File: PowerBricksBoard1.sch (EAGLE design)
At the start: 16 parts

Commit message: test
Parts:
- removed U$6: BRICKBOARD_TSW_14X2, Dist_to_Brickboard_Connector_brick:BRICKBOARD_TSW_14X2
- added U$2: BRICK2DIST, Brick_Dist_Connector:BRICK2DIST
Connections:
- net 12V: now also U$2.VOUT+; no longer U$6.45, U$6.46, U$6.47, U$6.48, U$6.49, U$6.50, U$6.51, U$6.52, U$6.53, U$6.54, U$6.55, U$6.56
- net 12_GND: now also U$2.VOUT-; no longer U$6.29, U$6.30, U$6.31, U$6.32, U$6.33, U$6.34, U$6.35, U$6.36, U$6.37, U$6.38, U$6.39, U$6.40
- net 48V: now also U$2.VIN+; no longer U$6.15, U$6.16, U$6.17, U$6.18, U$6.19, U$6.20, U$6.21, U$6.22, U$6.23, U$6.24, U$6.25, U$6.26, U$6.27, U$6.28
- net 48_GND: now also U$2.VIN-; no longer U$6.10, U$6.11, U$6.12, U$6.13, U$6.14, U$6.3, U$6.4, U$6.5, U$6.6, U$6.7, U$6.8, U$6.9
- net ALERT: now also U$2.ALERT; no longer U$6.43
- net CLK: now also U$2.CLK; no longer U$6.44
- net DATA: now also U$2.DATA; no longer U$6.42
- net ON/OFF: now also U$2.C2, U$2.ON/OFF; no longer U$6.1
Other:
- note added: "ADDR1 = R3 Resistor ADDR0 = R4 Resistor Octal Address = 8*ADDR1 + ADDR0 0-12 and 40, 44, 45, and 55 address can’t be used (decimal)"
- note added: "Backplane Connector"
- note added: "Brick Connections"
- note removed: "ADDR1 = R3 Resistor ADDR0 = R4 Resistor Octal Address = 8*ADDR1 + ADDR0"
- moved on the sheet: C1, C2, C3, D1, D2, H1, H2, H3, H4, R1, R2, R3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

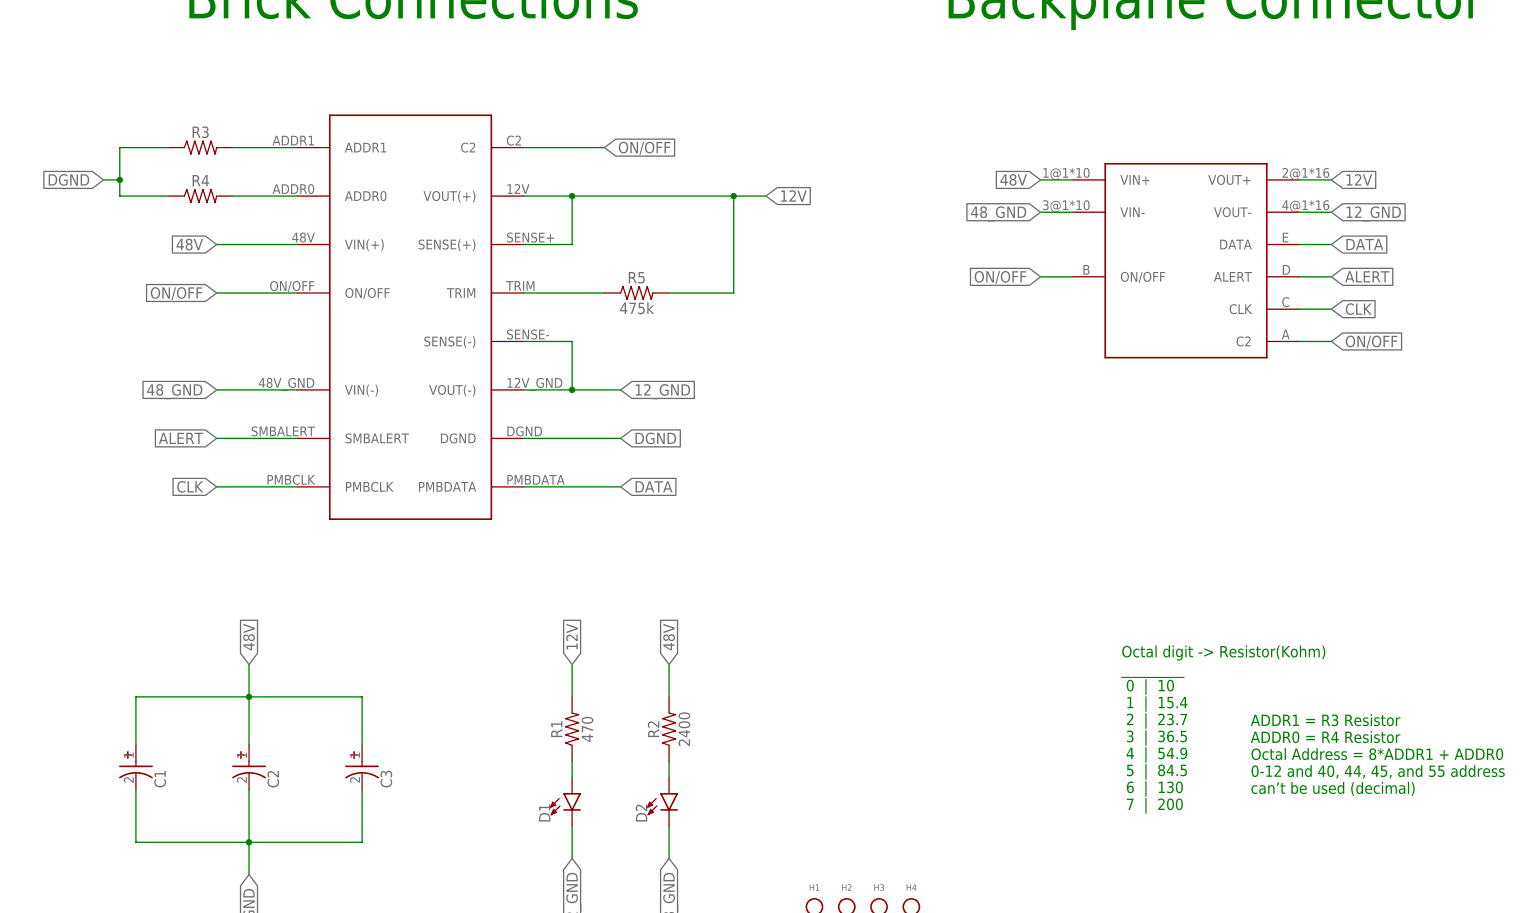
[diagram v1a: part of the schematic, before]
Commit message: cad placement for tyler (routing not done)
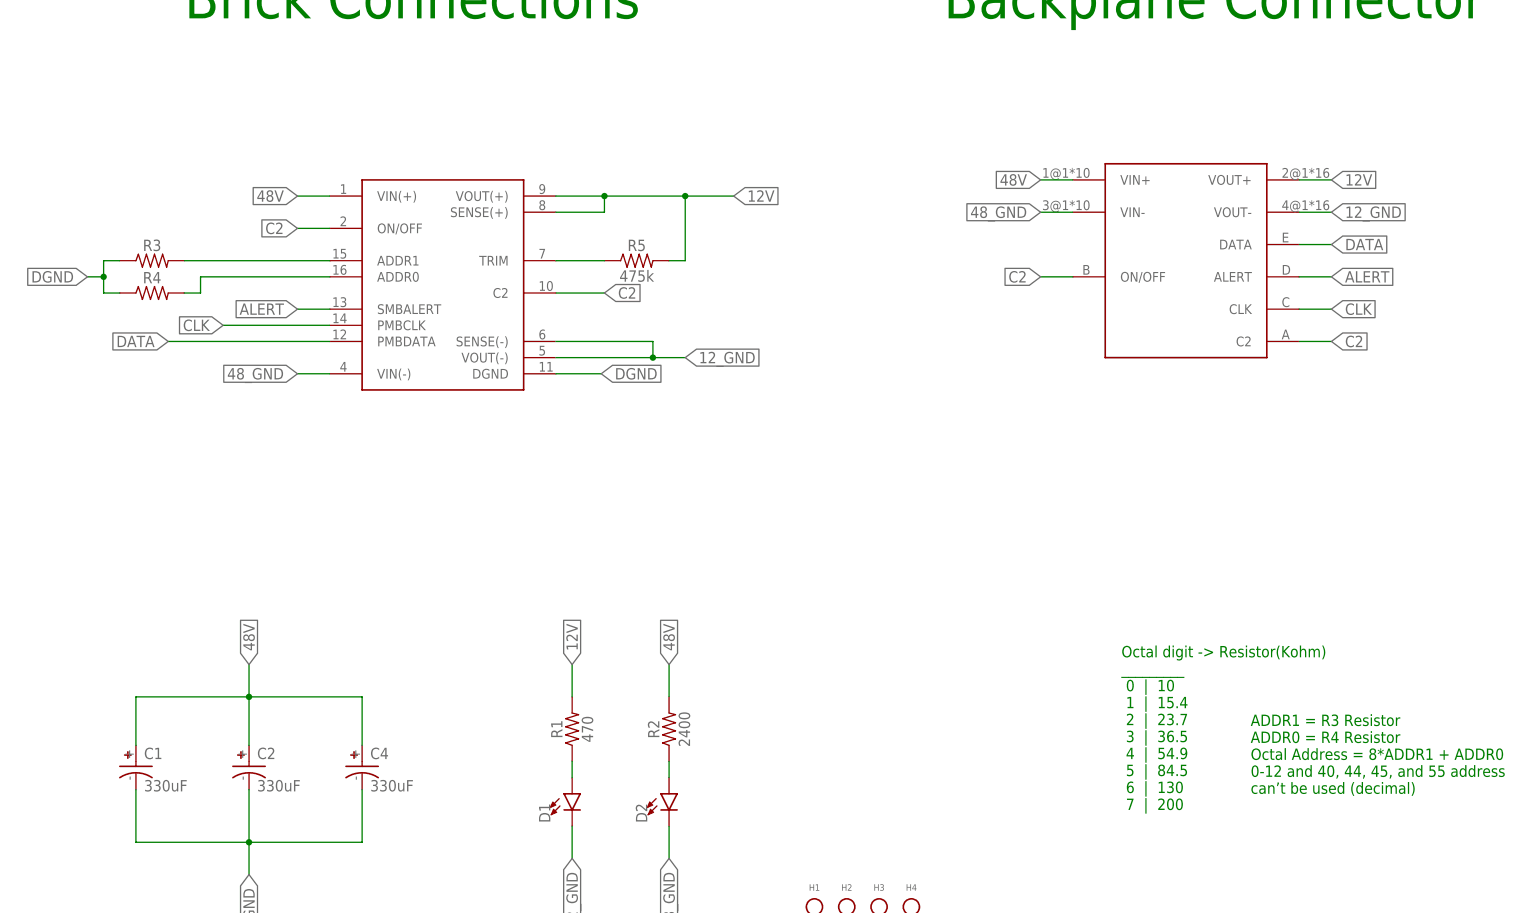
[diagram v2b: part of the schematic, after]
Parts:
- removed C3: UCM1H331MNL1GS, UCM1H331MNL1GS:UCM1H331MNL1GS
- removed U$1: Q48SC12050NRDH, Q48SC12050NRDH:Q48SC12050NRDH
- added C4: 330uF, brick-capacitor-UCM1H331MNL1GS:UCM1H331MNL1GS
- added U$3: BRICK2DIST_C, Brick_Dist_Connector:BRICK2DIST_C
- C1, C2: value UCM1H331MNL1GS -> 330uF; device UCM1H331MNL1GS:UCM1H331MNL1GS -> brick-capacitor-UCM1H331MNL1GS:UCM1H331MNL1GS
- U$2: value BRICK2DIST -> Q48SC12050NRDH; device Brick_Dist_Connector:BRICK2DIST -> Delta Power Bricks - Q48SC12050NRDH:Q48SC12050NRDH
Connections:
- removed net ON/OFF: U$1.C2, U$1.ON/OFF, U$2.C2, U$2.ON/OFF
- new net C2: U$2.C2, U$2.ON/OFF, U$3.C2, U$3.ON/OFF
- net 12V: now also U$2.SENSE(+), U$2.VOUT(+), U$3.VOUT+; no longer U$1.SENSE(+), U$1.VOUT(+), U$2.VOUT+
- net 12_GND: now also U$2.SENSE(-), U$2.VOUT(-), U$3.VOUT-; no longer U$1.SENSE(-), U$1.VOUT(-), U$2.VOUT-
- net 48V: now also C4.+, U$2.VIN(+), U$3.VIN+; no longer C3.+, U$1.VIN(+), U$2.VIN+
- net 48_GND: now also C4.-, U$2.VIN(-), U$3.VIN-; no longer C3.-, U$1.VIN(-), U$2.VIN-
- net ALERT: now also U$2.SMBALERT, U$3.ALERT; no longer U$1.SMBALERT, U$2.ALERT
- net CLK: now also U$2.PMBCLK, U$3.CLK; no longer U$1.PMBCLK, U$2.CLK
- net DATA: now also U$2.PMBDATA, U$3.DATA; no longer U$1.PMBDATA, U$2.DATA
- net DGND: now also U$2.DGND; no longer U$1.DGND
- net N$3: now also U$2.ADDR1; no longer U$1.ADDR1
- net N$4: now also U$2.ADDR0; no longer U$1.ADDR0
- net N$5: now also U$2.TRIM; no longer U$1.TRIM
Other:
- moved on the sheet: C1, C2, R3, R4, R5

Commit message: Owo
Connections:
- new net ON/OFF: U$2.ON/OFF, U$3.ON/OFF
- net C2: no longer U$2.ON/OFF, U$3.ON/OFF
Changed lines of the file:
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@@
 <net name="C2" class="0">
-<segment>
-<wire x1="48.26" y1="35.56" x2="43.18" y2="35.56" width="0.1524" layer="91"/>
-<label x="43.18" y="35.56" size="1.778" layer="95" rot="R180" xref="yes"/>
-<pinref part="U$3" gate="G$1" pin="ON/OFF"/>
-</segment>
 <segment>
 <wire x1="83.82" y1="25.4" x2="88.9" y2="25.4" width="0.1524" layer="91"/>
@@
 <label x="-25.4" y="33.02" size="1.778" layer="95" xref="yes"/>
 <pinref part="U$2" gate="G$1" pin="C2"/>
-</segment>
-<segment>
-<wire x1="-68.58" y1="43.18" x2="-73.66" y2="43.18" width="0.1524" layer="91"/>
-<label x="-73.66" y="43.18" size="1.778" layer="95" rot="R180" xref="yes"/>
-<pinref part="U$2" gate="G$1" pin="ON/OFF"/>
 </segment>
 </net>
@@
 </segment>
 </net>
+<net name="ON/OFF" class="0">
+<segment>
+<wire x1="-68.58" y1="43.18" x2="-73.66" y2="43.18" width="0.1524" layer="91"/>
+<label x="-73.66" y="43.18" size="1.778" layer="95" rot="R180" xref="yes"/>
+<pinref part="U$2" gate="G$1" pin="ON/OFF"/>
+</segment>
+<segment>
+<wire x1="48.26" y1="35.56" x2="43.18" y2="35.56" width="0.1524" layer="91"/>
+<label x="43.18" y="35.56" size="1.778" layer="95" rot="R180" xref="yes"/>
+<pinref part="U$3" gate="G$1" pin="ON/OFF"/>
+</segment>
+</net>

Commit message: Done but I still need to add a picture Owo
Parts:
- removed U$3: BRICK2DIST_C, Brick_Dist_Connector:BRICK2DIST_C
- added U$1: BRICK2DIST, Brick_Dist_Connector:BRICK2DIST
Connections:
- net 12V: now also U$1.VOUT+; no longer U$3.VOUT+
- net 12_GND: now also U$1.VOUT-; no longer U$3.VOUT-
- net 48V: now also U$1.VIN+; no longer U$3.VIN+
- net 48_GND: now also U$1.VIN-; no longer U$3.VIN-
- net ALERT: now also U$1.ALERT; no longer U$3.ALERT
- net C2: now also U$1.C2; no longer U$3.C2
- net CLK: now also U$1.CLK; no longer U$3.CLK
- net DATA: now also U$1.DATA; no longer U$3.DATA
- net ON/OFF: now also U$1.ON/OFF; no longer U$3.ON/OFF
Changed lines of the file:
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@@
 <part name="H3" library="Mounting Holes" deviceset="6-32-HOLE" device="" package3d_urn="urn:adsk.eagle:package:24384748/2"/>
 <part name="H4" library="Mounting Holes" deviceset="6-32-HOLE" device="" package3d_urn="urn:adsk.eagle:package:24384748/2"/>
-<part name="U$3" library="Brick_Dist_Connector" deviceset="BRICK2DIST_C" device=""/>
 <part name="C1" library="brick-capacitor-UCM1H331MNL1GS" deviceset="UCM1H331MNL1GS" device="" package3d_urn="urn:adsk.eagle:package:24202090/2" value="330uF"/>
 <part name="C2" library="brick-capacitor-UCM1H331MNL1GS" deviceset="UCM1H331MNL1GS" device="" package3d_urn="urn:adsk.eagle:package:24202090/2" value="330uF"/>
@@
 <part name="R3" library="SparkFun-Resistors" library_urn="urn:adsk.eagle:library:532" deviceset="RESISTOR" device="0603" package3d_urn="urn:adsk.eagle:package:39650/1" value=" "/>
 <part name="R5" library="SparkFun-Resistors" library_urn="urn:adsk.eagle:library:532" deviceset="RESISTOR" device="0603" package3d_urn="urn:adsk.eagle:package:39650/1" value="475k"/>
+<part name="U$1" library="Brick_Dist_Connector" deviceset="BRICK2DIST" device=""/>
 </parts>
 <sheets>
@@
 <attribute name="VALUE" x="22.86" y="-66.04" size="1.016" layer="95" align="top-center"/>
 </instance>
-<instance part="U$3" gate="G$1" x="53.34" y="45.72" smashed="yes"/>
 <instance part="C1" gate="G$1" x="-99.06" y="-40.64" smashed="yes">
 <attribute name="NAME" x="-97.79" y="-39.37" size="1.778" layer="95" align="center-left"/>
@@
 <attribute name="NAME" x="-20.32" y="39.624" size="1.778" layer="95" font="vector" align="bottom-center"/>
 <attribute name="VALUE" x="-20.32" y="36.576" size="1.778" layer="96" font="vector" align="top-center"/>
+</instance>
+<instance part="U$1" gate="G$1" x="53.34" y="45.72" smashed="yes">
+<attribute name="NAME" x="53.848" y="54.356" size="1.778" layer="95"/>
 </instance>
 </instances>
@@
 <wire x1="48.26" y1="50.8" x2="43.18" y2="50.8" width="0.1524" layer="91"/>
 <label x="43.18" y="50.8" size="1.778" layer="95" rot="R180" xref="yes"/>
-<pinref part="U$3" gate="G$1" pin="VIN+"/>
+<pinref part="U$1" gate="G$1" pin="VIN+"/>
 </segment>
 <segment>
@@
 <wire x1="48.26" y1="45.72" x2="43.18" y2="45.72" width="0.1524" layer="91"/>
 <label x="43.18" y="45.72" size="1.778" layer="95" rot="R180" xref="yes"/>
-<pinref part="U$3" gate="G$1" pin="VIN-"/>
+<pinref part="U$1" gate="G$1" pin="VIN-"/>
 </segment>
 <segment>
@@
 <wire x1="83.82" y1="50.8" x2="88.9" y2="50.8" width="0.1524" layer="91"/>
 <label x="88.9" y="50.8" size="1.778" layer="95" xref="yes"/>
-<pinref part="U$3" gate="G$1" pin="VOUT+"/>
+<pinref part="U$1" gate="G$1" pin="VOUT+"/>
 </segment>
 <segment>
@@
 <wire x1="83.82" y1="25.4" x2="88.9" y2="25.4" width="0.1524" layer="91"/>
 <label x="88.9" y="25.4" size="1.778" layer="95" xref="yes"/>
-<pinref part="U$3" gate="G$1" pin="C2"/>
+<pinref part="U$1" gate="G$1" pin="C2"/>
 </segment>
 <segment>
@@
 <wire x1="83.82" y1="45.72" x2="88.9" y2="45.72" width="0.1524" layer="91"/>
 <label x="88.9" y="45.72" size="1.778" layer="95" xref="yes"/>
-<pinref part="U$3" gate="G$1" pin="VOUT-"/>
+<pinref part="U$1" gate="G$1" pin="VOUT-"/>
 </segment>
 <segment>
@@
 <wire x1="83.82" y1="35.56" x2="88.9" y2="35.56" width="0.1524" layer="91"/>
 <label x="88.9" y="35.56" size="1.778" layer="95" xref="yes"/>
-<pinref part="U$3" gate="G$1" pin="ALERT"/>
+<pinref part="U$1" gate="G$1" pin="ALERT"/>
 </segment>
 <segment>
@@
 <wire x1="83.82" y1="40.64" x2="88.9" y2="40.64" width="0.1524" layer="91"/>
 <label x="88.9" y="40.64" size="1.778" layer="95" xref="yes"/>
-<pinref part="U$3" gate="G$1" pin="DATA"/>
+<pinref part="U$1" gate="G$1" pin="DATA"/>
 </segment>
 <segment>
@@
 <wire x1="83.82" y1="30.48" x2="88.9" y2="30.48" width="0.1524" layer="91"/>
 <label x="88.9" y="30.48" size="1.778" layer="95" xref="yes"/>
-<pinref part="U$3" gate="G$1" pin="CLK"/>
+<pinref part="U$1" gate="G$1" pin="CLK"/>
 </segment>
 <segment>
@@
 <wire x1="48.26" y1="35.56" x2="43.18" y2="35.56" width="0.1524" layer="91"/>
 <label x="43.18" y="35.56" size="1.778" layer="95" rot="R180" xref="yes"/>
-<pinref part="U$3" gate="G$1" pin="ON/OFF"/>
-</segment>
-</net>
+<pinref part="U$1" gate="G$1" pin="ON/OFF"/>
+</segment>
+</net>

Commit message: owo
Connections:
- net 48V renamed 48V_GND
- net N$3 renamed ADDR1
- net N$4 renamed ADDR0
- net N$5 renamed TRIM
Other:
- note added: "Trim up: 5.11 * 12 (100+ Delta )/(1.225* Delta) - 511/Delta - 10.2 = resistor to use in kOhm Where Delta is the % up for trim (10% = 10)"
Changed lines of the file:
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@@
 <text x="-91.44" y="76.2" size="6.4516" layer="91">Brick Connections</text>
 <text x="27.94" y="76.2" size="6.4516" layer="91">Backplane Connector</text>
+<text x="55.88" y="-17.78" size="1.778" layer="91">Trim up: 5.11 * 12 (100+ Delta )/(1.225* Delta)
+- 511/Delta - 10.2 = resistor to use in kOhm
+Where Delta is the % up for trim (10% = 10) </text>
 </plain>
 <instances>
@@
 </busses>
 <nets>
-<net name="48V" class="0">
+<net name="48V_GND" class="0">
 <segment>
 <wire x1="-99.06" y1="-30.48" x2="-81.28" y2="-30.48" width="0.1524" layer="91"/>
@@
 </segment>
 </net>
-<net name="N$3" class="0">
+<net name="ADDR1" class="0">
 <segment>
 <wire x1="-91.44" y1="38.1" x2="-68.58" y2="38.1" width="0.1524" layer="91"/>
 <pinref part="R3" gate="G$1" pin="2"/>
 <pinref part="U$2" gate="G$1" pin="ADDR1"/>
-</segment>
-</net>
-<net name="N$4" class="0">
+<label x="-88.9" y="38.1" size="1.778" layer="95"/>
+</segment>
+</net>
+<net name="ADDR0" class="0">
 <segment>
 <pinref part="U$2" gate="G$1" pin="ADDR0"/>
@@
 <pinref part="R4" gate="G$1" pin="2"/>
 <wire x1="-88.9" y1="33.02" x2="-91.44" y2="33.02" width="0.1524" layer="91"/>
-</segment>
-</net>
-<net name="N$5" class="0">
+<label x="-88.9" y="35.56" size="1.778" layer="95"/>
+</segment>
+</net>
+<net name="TRIM" class="0">
 <segment>
 <wire x1="-25.4" y1="38.1" x2="-33.02" y2="38.1" width="0.1524" layer="91"/>
 <pinref part="R5" gate="G$1" pin="1"/>
 <pinref part="U$2" gate="G$1" pin="TRIM"/>
-</segment>
-</net>
+<label x="-31.75" y="38.1" size="1.778" layer="95"/>
+</segment>
+</net>

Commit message: trim
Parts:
- R5: value 475k -> 510k
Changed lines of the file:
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@@
 <part name="R4" library="SparkFun-Resistors" library_urn="urn:adsk.eagle:library:532" deviceset="RESISTOR" device="0603" package3d_urn="urn:adsk.eagle:package:39650/1" value=" "/>
 <part name="R3" library="SparkFun-Resistors" library_urn="urn:adsk.eagle:library:532" deviceset="RESISTOR" device="0603" package3d_urn="urn:adsk.eagle:package:39650/1" value=" "/>
-<part name="R5" library="SparkFun-Resistors" library_urn="urn:adsk.eagle:library:532" deviceset="RESISTOR" device="0603" package3d_urn="urn:adsk.eagle:package:39650/1" value="475k"/>
+<part name="R5" library="SparkFun-Resistors" library_urn="urn:adsk.eagle:library:532" deviceset="RESISTOR" device="0603" package3d_urn="urn:adsk.eagle:package:39650/1" value="510k"/>
 <part name="U$1" library="Brick_Dist_Connector" deviceset="BRICK2DIST" device=""/>
 </parts>

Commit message: Cleaning up git and exports for order
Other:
- moved on the sheet: C1, C2, C4, D1, D2, H1, H2, H3, H4, R1, R2, R3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

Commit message: euhreiuhthjtrgrefwefrgyjgr
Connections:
- net 48V_GND renamed 48V
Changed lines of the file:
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@@
 </busses>
 <nets>
-<net name="48V_GND" class="0">
-<segment>
-<wire x1="30.48" y1="48.26" x2="48.26" y2="48.26" width="0.1524" layer="91"/>
-<wire x1="48.26" y1="48.26" x2="66.04" y2="48.26" width="0.1524" layer="91"/>
-<junction x="48.26" y="48.26"/>
-<wire x1="48.26" y1="48.26" x2="48.26" y2="53.34" width="0.1524" layer="91"/>
-<label x="48.26" y="53.34" size="1.778" layer="95" rot="R90" xref="yes"/>
-<pinref part="C1" gate="G$1" pin="+"/>
-<wire x1="30.48" y1="48.26" x2="30.48" y2="40.64" width="0.1524" layer="91"/>
-<pinref part="C2" gate="G$1" pin="+"/>
-<wire x1="48.26" y1="48.26" x2="48.26" y2="40.64" width="0.1524" layer="91"/>
-<pinref part="C4" gate="G$1" pin="+"/>
-<wire x1="66.04" y1="48.26" x2="66.04" y2="40.64" width="0.1524" layer="91"/>
-</segment>
-<segment>
-<wire x1="114.3" y1="48.26" x2="114.3" y2="53.34" width="0.1524" layer="91"/>
-<label x="114.3" y="53.34" size="1.778" layer="95" rot="R90" xref="yes"/>
-<pinref part="R2" gate="G$1" pin="2"/>
-</segment>
-<segment>
-<wire x1="177.8" y1="129.54" x2="172.72" y2="129.54" width="0.1524" layer="91"/>
-<label x="172.72" y="129.54" size="1.778" layer="95" rot="R180" xref="yes"/>
-<pinref part="U$1" gate="G$1" pin="VIN+"/>
-</segment>
-<segment>
-<wire x1="60.96" y1="127" x2="55.88" y2="127" width="0.1524" layer="91"/>
-<label x="55.88" y="127" size="1.778" layer="95" rot="R180" xref="yes"/>
-<pinref part="U$2" gate="G$1" pin="VIN(+)"/>
-</segment>
-</net>
 <net name="48_GND" class="0">
 <segment>
@@
 </segment>
 </net>
+<net name="48V" class="0">
+<segment>
+<wire x1="60.96" y1="127" x2="55.88" y2="127" width="0.1524" layer="91"/>
+<label x="55.88" y="127" size="1.778" layer="95" rot="R180" xref="yes"/>
+<pinref part="U$2" gate="G$1" pin="VIN(+)"/>
+</segment>
+<segment>
+<wire x1="177.8" y1="129.54" x2="172.72" y2="129.54" width="0.1524" layer="91"/>
+<label x="172.72" y="129.54" size="1.778" layer="95" rot="R180" xref="yes"/>
+<pinref part="U$1" gate="G$1" pin="VIN+"/>
+</segment>
+<segment>
+<wire x1="30.48" y1="48.26" x2="48.26" y2="48.26" width="0.1524" layer="91"/>
+<wire x1="48.26" y1="48.26" x2="66.04" y2="48.26" width="0.1524" layer="91"/>
+<junction x="48.26" y="48.26"/>
+<wire x1="48.26" y1="48.26" x2="48.26" y2="53.34" width="0.1524" layer="91"/>
+<label x="48.26" y="53.34" size="1.778" layer="95" rot="R90" xref="yes"/>
+<pinref part="C1" gate="G$1" pin="+"/>
+<wire x1="30.48" y1="48.26" x2="30.48" y2="40.64" width="0.1524" layer="91"/>
+<pinref part="C2" gate="G$1" pin="+"/>
+<wire x1="48.26" y1="48.26" x2="48.26" y2="40.64" width="0.1524" layer="91"/>
+<pinref part="C4" gate="G$1" pin="+"/>
+<wire x1="66.04" y1="48.26" x2="66.04" y2="40.64" width="0.1524" layer="91"/>
+</segment>
+<segment>
+<wire x1="114.3" y1="48.26" x2="114.3" y2="53.34" width="0.1524" layer="91"/>
+<label x="114.3" y="53.34" size="1.778" layer="95" rot="R90" xref="yes"/>
+<pinref part="R2" gate="G$1" pin="2"/>
+</segment>
+</net>
